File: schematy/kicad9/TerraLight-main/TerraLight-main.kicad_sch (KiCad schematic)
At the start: 66 parts, among them J1 USB-C 16P ≥3A, J2 LED OUT (JST-VH 3p), J3 SENSOR (JST-GH 6p), J4 PROG UART (pady), J5 Rezerwa (pady), Q1 P-MOSFET ≤30mΩ, Q2 2N7002, SW1 BOOT, SW2 RESET, U1 74AHCT1G125, U2 SRV05-4, U3 USBLC6-2SC6, U4 AP2112K-3.3, U5 ESP32-C3-MINI-1-N4

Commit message: schematy: 0805 passives for hand assembly, MPN fields, BOM for 5 prototypes
Prototypes will be assembled by hand (stencil + hot air), so all small
passives move from 0402 to 0805 and the status LED to 0805. Every part
gets an MPN field; BOM_prototyp_5szt.csv lists quantities for a batch of
five with spares. Connectivity unchanged (53 nets, 0 unconnected).

Co-Authored-By: Claude Opus 5.5 <noreply@anthropic.com>
Claude-Session: https://claude.ai/code/session_011xrhtcpPCLVqz5j5FtXSAa
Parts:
- C1, C11, C6: MPN (none) -> Samsung CL21A106KAYNNNE
- C10, C13, C9: footprint Capacitor_SMD:C_0402_1005Metric -> Capacitor_SMD:C_0805_2012Metric; MPN (none) -> Samsung CL21B105KAFNNNE
- C12, C3, C8: footprint Capacitor_SMD:C_0402_1005Metric -> Capacitor_SMD:C_0805_2012Metric; MPN (none) -> Samsung CL21B104KBCNNNC
- C2, C7: MPN (none) -> [100 µF ≥10 V, SMD Ø6,3 mm]
- C4: footprint Capacitor_SMD:C_0402_1005Metric -> Capacitor_SMD:C_0805_2012Metric; MPN (none) -> Samsung CL21B223KBANNNC
- C5: MPN (none) -> [1000 µF 10 V low-ESR, SMD Ø10 mm]
- D1: MPN (none) -> Littelfuse SMF5.0A
- D2: MPN (none) -> Nexperia PESD5V0S1BA
- D3: MPN (none) -> SS14
- F1: MPN (none) -> Bourns MF-MSMF300-2 [lub inny PTC 1812, 3 A hold, ≥6 V]
- F2: MPN (none) -> Littelfuse 0805L010
- J1: MPN (none) -> HRO TYPE-C-31-M-12
- J2: MPN (none) -> JST S3P-VH(LF)(SN)
- J3: MPN (none) -> JST SM06B-GHS-TB(LF)(SN)
- J4: MPN (none) -> [listwa 1×6 2,54 mm — opcjonalnie]
- J5: MPN (none) -> [listwa 1×4 2,54 mm — opcjonalnie]
- LED1: footprint LED_SMD:LED_0603_1608Metric -> LED_SMD:LED_0805_2012Metric; MPN (none) -> [LED 0805, dowolny kolor]
- Q1: MPN (none) -> Vishay Si2333DDS [sprawdzić RDS(on) i pinout]
- Q2: MPN (none) -> 2N7002
- R1, R2: footprint Resistor_SMD:R_0402_1005Metric -> Resistor_SMD:R_0805_2012Metric; MPN (none) -> Yageo RC0805FR-075K1L
- R10, R11, R15, R9: footprint Resistor_SMD:R_0402_1005Metric -> Resistor_SMD:R_0805_2012Metric; MPN (none) -> Yageo RC0805FR-071KL
- R12, R13, R14, R16, R6: footprint Resistor_SMD:R_0402_1005Metric -> Resistor_SMD:R_0805_2012Metric; MPN (none) -> Yageo RC0805FR-0710KL
- R17, R18, R19, R20: footprint Resistor_SMD:R_0402_1005Metric -> Resistor_SMD:R_0805_2012Metric; MPN (none) -> Yageo RC0805FR-07100RL
- R21, R22, R23, R24: footprint Resistor_SMD:R_0402_1005Metric -> Resistor_SMD:R_0805_2012Metric; MPN (none) -> Yageo RC0805FR-074K7L
- R3, R5, R7: footprint Resistor_SMD:R_0402_1005Metric -> Resistor_SMD:R_0805_2012Metric; MPN (none) -> Yageo RC0805FR-07100KL
- R4: footprint Resistor_SMD:R_0402_1005Metric -> Resistor_SMD:R_0805_2012Metric; MPN (none) -> Yageo RC0805FR-0747KL
- R8: footprint Resistor_SMD:R_0402_1005Metric -> Resistor_SMD:R_0805_2012Metric; MPN (none) -> Yageo RC0805FR-07330RL
- SW1, SW2: MPN (none) -> E-Switch TL3342 [sprawdzić wariant]
- U1: MPN (none) -> TI SN74AHCT1G125DBVR
- U2: MPN (none) -> Semtech SRV05-4
- U3: MPN (none) -> ST USBLC6-2SC6
- U4: MPN (none) -> Diodes AP2112K-3.3TRG1
- U5: MPN (none) -> Espressif ESP32-C3-MINI-1-N4

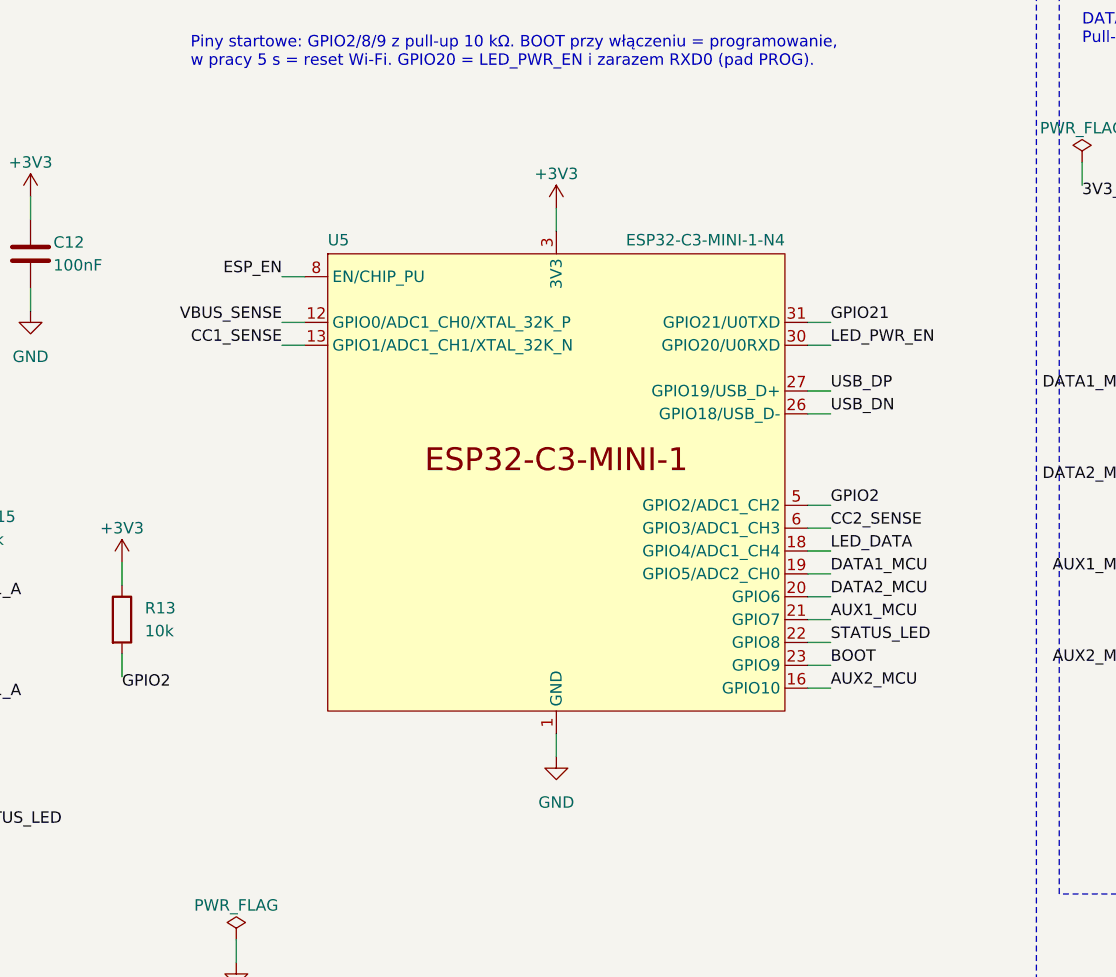
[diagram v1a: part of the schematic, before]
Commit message: schematy: ESP32-C3-WROOM-02 for hand-soldered prototypes
The owner assembles the first boards by hand, so the module changes from
ESP32-C3-MINI-1 (pads only underneath, needs hot air) to
ESP32-C3-WROOM-02-N4 with castellated edge pads. The footprint is
Espressif's with one plated hole in the GND pad so it can be soldered
from the bottom with an iron. GPIO assignment is unchanged (checked pin
by pin against docs/PCB.md); firmware needs no changes.

Co-Authored-By: Claude Opus 5.5 <noreply@anthropic.com>
Claude-Session: https://claude.ai/code/session_011xrhtcpPCLVqz5j5FtXSAa
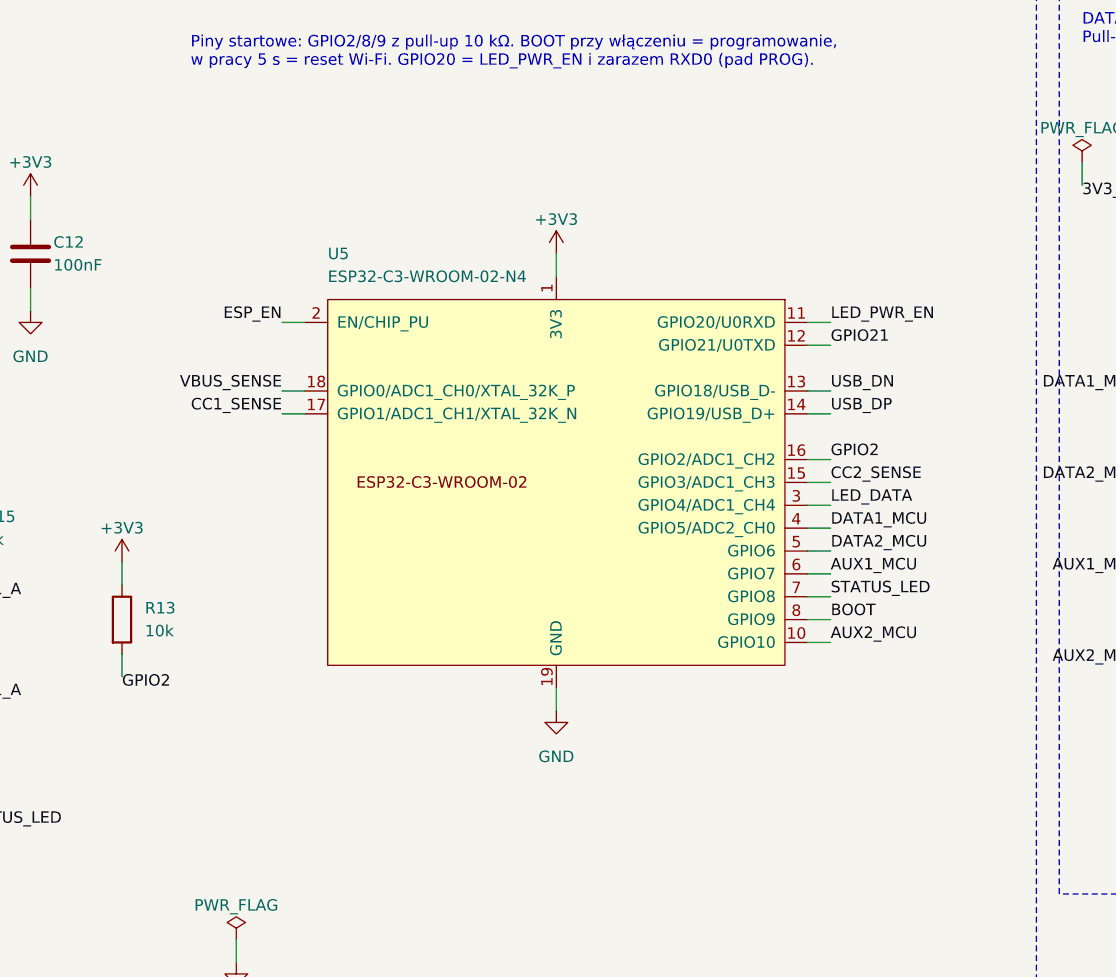
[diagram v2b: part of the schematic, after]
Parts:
- U5: value ESP32-C3-MINI-1-N4 -> ESP32-C3-WROOM-02-N4; footprint TerraLight:ESP32-C3-MINI-1 -> TerraLight:ESP32-C3-WROOM-02_HandSolder; symbol TerraLight:ESP32-C3-MINI-1 -> TerraLight:ESP32-C3-WROOM-02; MPN Espressif ESP32-C3-MINI-1-N4 -> Espressif ESP32-C3-WROOM-02-N4; Uwagi antena wbudowana; strefa bez miedzi wg karty -> antena PCB na krawędzi płytki — strefa bez miedzi wg karty;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
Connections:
- net +3V3: now also U5.1 (3V3); no longer U5.3 (3V3)
- net AUX1_MCU: now also U5.6 (GPIO7); no longer U5.21 (GPIO7)
- net AUX2_MCU: now also U5.10 (GPIO10); no longer U5.16 (GPIO10)
- net BOOT: now also U5.8 (GPIO9); no longer U5.23 (GPIO9)
- net CC1_SENSE: now also U5.17 (GPIO1/ADC1_CH1/XTAL_32K_N); no longer U5.13 (GPIO1/ADC1_CH1/XTAL_32K_N)
- net CC2_SENSE: now also U5.15 (GPIO3/ADC1_CH3); no longer U5.6 (GPIO3/ADC1_CH3)
- net DATA1_MCU: now also U5.4 (GPIO5/ADC2_CH0); no longer U5.19 (GPIO5/ADC2_CH0)
- net DATA2_MCU: now also U5.5 (GPIO6); no longer U5.20 (GPIO6)
- net ESP_EN: now also U5.2 (EN/CHIP_PU); no longer U5.8 (EN/CHIP_PU)
- net GND: now also U5.19 (GND), U5.9 (GND); no longer U5.1 (GND), U5.11 (GND), U5.14 (GND), U5.2 (GND), U5.36 (GND), U5.37 (GND), U5.38 (GND), U5.39 (GND), U5.40 (GND), U5.41 (GND), U5.42 (GND), U5.43 (GND), U5.44 (GND), U5.45 (GND), U5.46 (GND), U5.47 (GND), U5.48 (GND), U5.49 (GND), U5.50 (GND), U5.51 (GND), U5.52 (GND), U5.53 (GND)
- net GPIO2: now also U5.16 (GPIO2/ADC1_CH2); no longer U5.5 (GPIO2/ADC1_CH2)
- net GPIO21: now also U5.12 (GPIO21/U0TXD); no longer U5.31 (GPIO21/U0TXD)
- net LED_DATA: now also U5.3 (GPIO4/ADC1_CH4); no longer U5.18 (GPIO4/ADC1_CH4)
- net LED_PWR_EN: now also U5.11 (GPIO20/U0RXD); no longer U5.30 (GPIO20/U0RXD)
- net STATUS_LED: now also U5.7 (GPIO8); no longer U5.22 (GPIO8)
- net USB_DN: now also U5.13 (GPIO18/USB_D-); no longer U5.26 (GPIO18/USB_D-)
- net USB_DP: now also U5.14 (GPIO19/USB_D+); no longer U5.27 (GPIO19/USB_D+)
- net VBUS_SENSE: now also U5.18 (GPIO0/ADC1_CH0/XTAL_32K_P); no longer U5.12 (GPIO0/ADC1_CH0/XTAL_32K_P)
